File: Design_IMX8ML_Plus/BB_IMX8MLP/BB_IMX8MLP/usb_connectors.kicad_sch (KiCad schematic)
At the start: 29 parts, among them J9 GSB311231HR, P1 USB_C_Plug, U10 PCMF3USB3S, U9 PCMF3USB3S

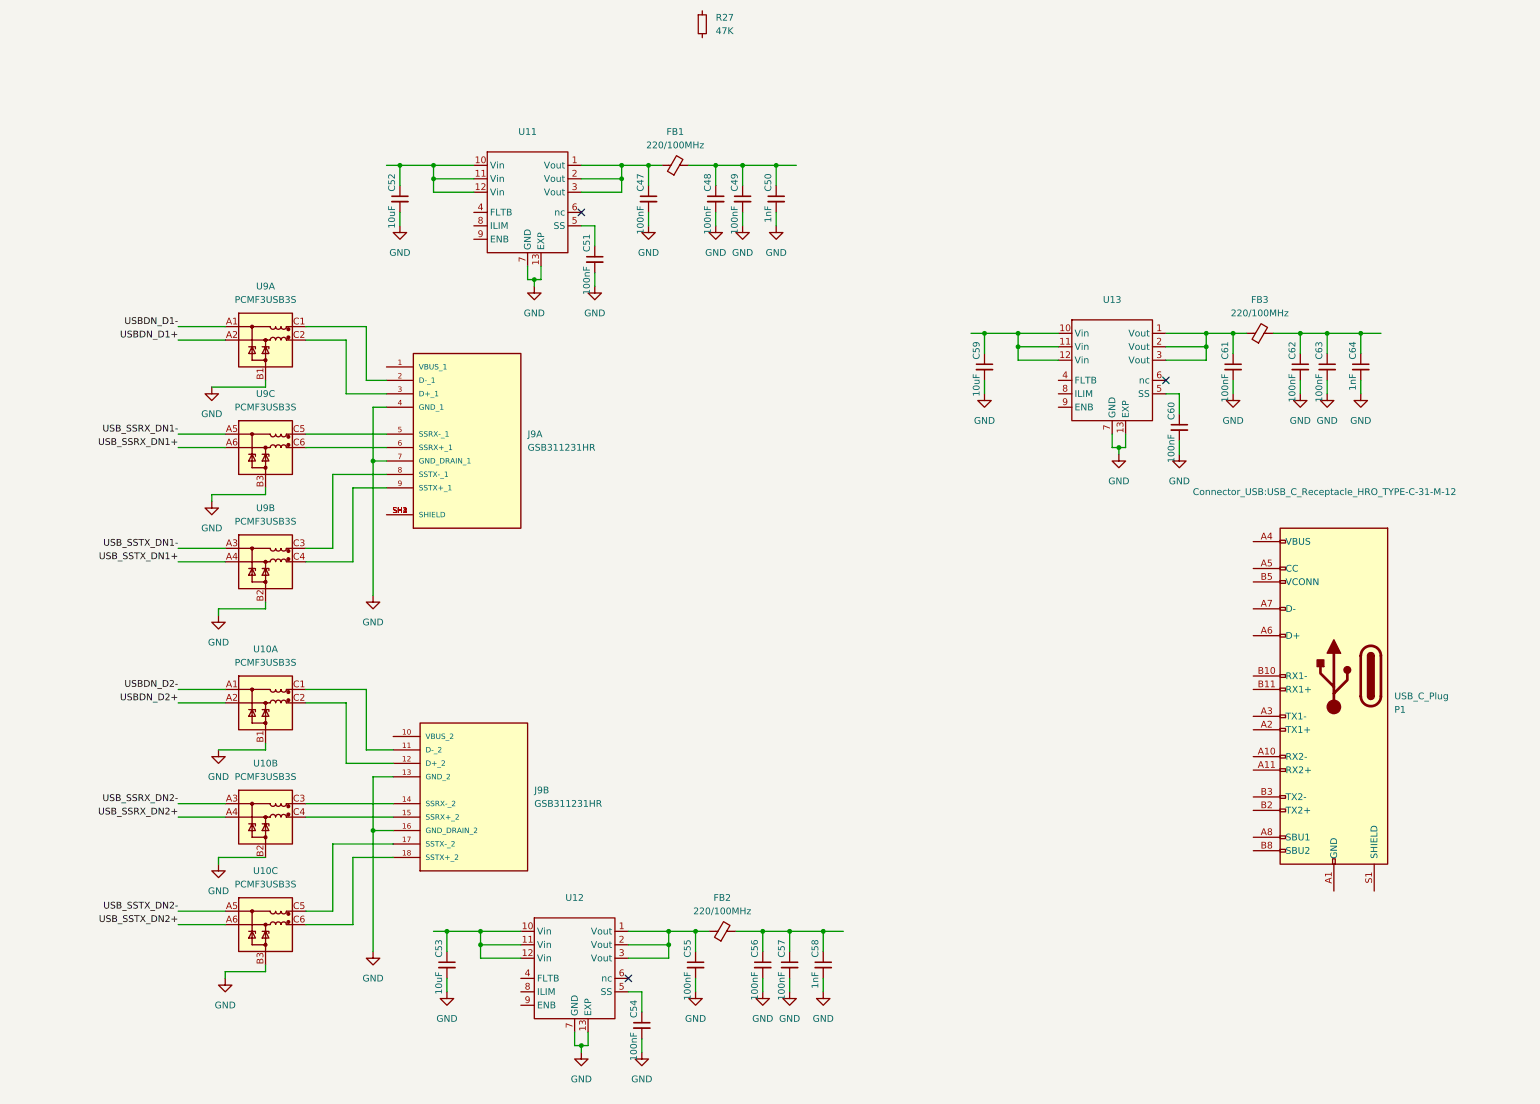
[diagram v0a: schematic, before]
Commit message: improving Ethernet, USB and Camera inteface
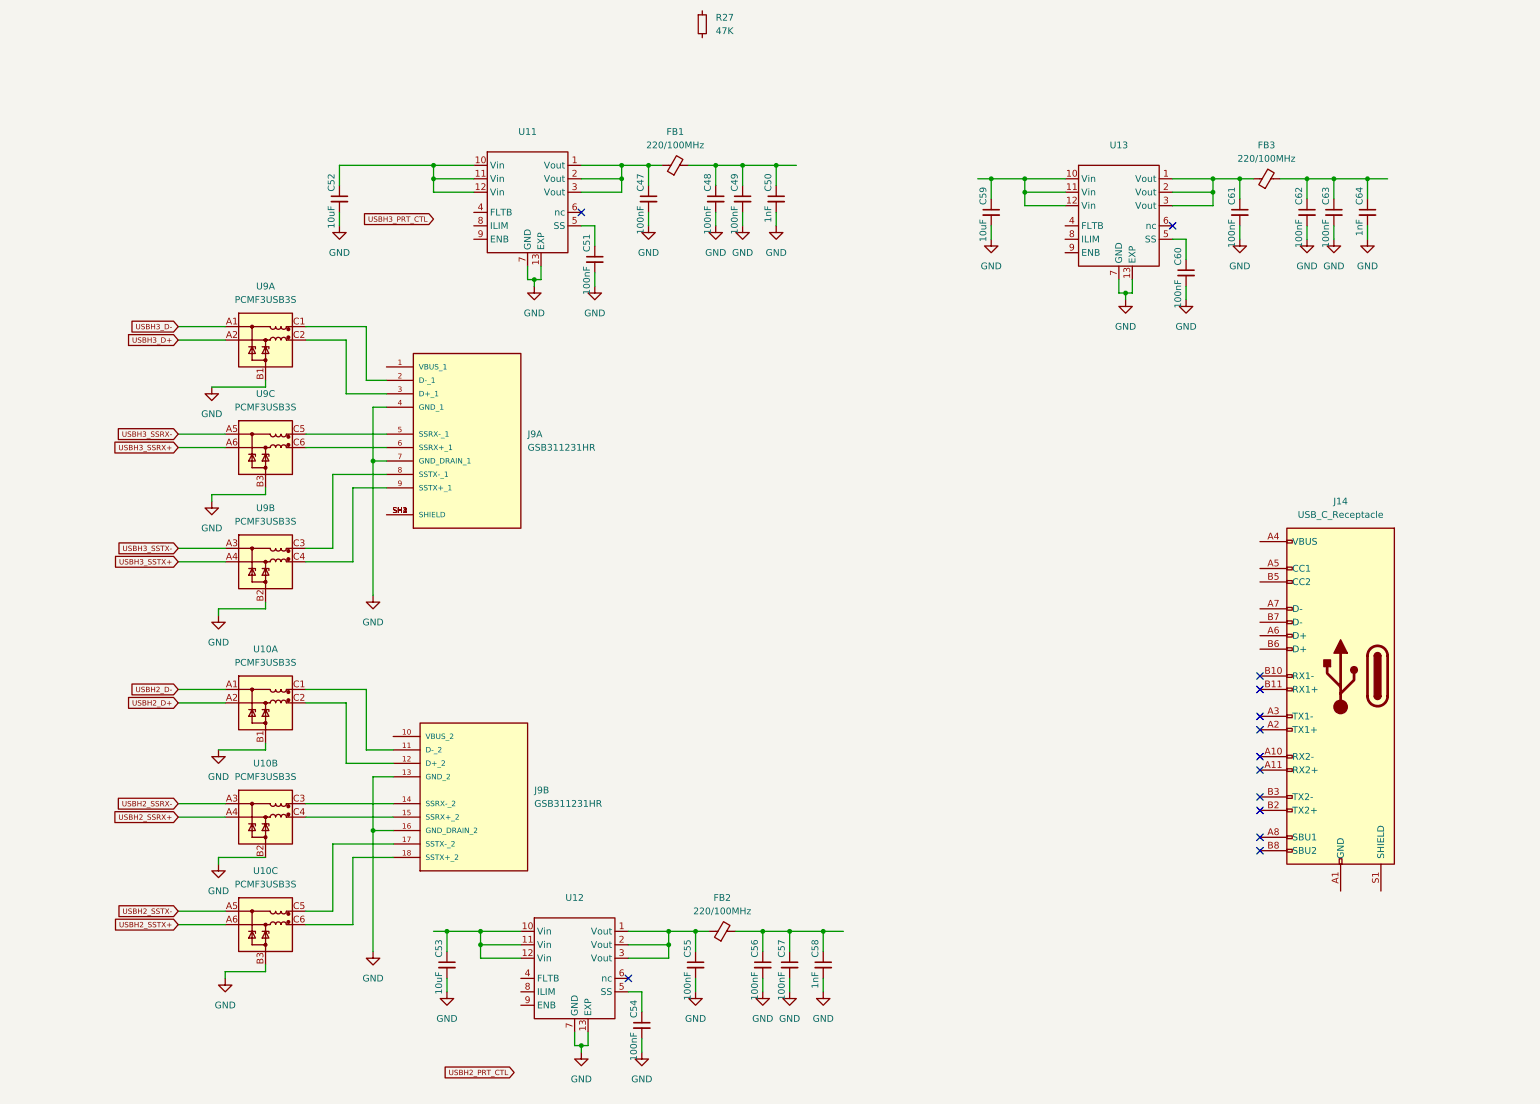
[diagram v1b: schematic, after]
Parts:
- removed P1: USB_C_Plug, Connector_USB:USB_C_Receptacle_HRO_TYPE-C-31-M-12, symbol Connector:USB_C_Plug
- added J14: USB_C_Receptacle, symbol Connector:USB_C_Receptacle
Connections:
- net USBDN_D1+ renamed USBH3_D+
- net USBDN_D1- renamed USBH3_D-
- net USBDN_D2+ renamed USBH2_D+
- net USBDN_D2- renamed USBH2_D-
- net USB_SSRX_DN1+ renamed USBH3_SSRX+
- net USB_SSRX_DN1- renamed USBH3_SSRX-
- net USB_SSRX_DN2+ renamed USBH2_SSRX+
- net USB_SSRX_DN2- renamed USBH2_SSRX-
- net USB_SSTX_DN1+ renamed USBH3_SSTX+
- net USB_SSTX_DN1- renamed USBH3_SSTX-
- net USB_SSTX_DN2+ renamed USBH2_SSTX+
- net USB_SSTX_DN2- renamed USBH2_SSTX-
- new net: J14.A1 (GND), J14.A12 (GND), J14.B1 (GND), J14.B12 (GND)
- new net: J14.A4 (VBUS), J14.A9 (VBUS), J14.B4 (VBUS), J14.B9 (VBUS)
- no-connect marks 3 -> 13
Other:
- moved on the sheet: C52, C59, C60, C61, C62, C63, C64, FB3, U13

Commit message: Review
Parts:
- added C150, C151, C152, C153: 100nF, Capacitor_SMD:C_0402_1005Metric, symbol Device:C_Small
- added R59, R60, R61: 0, Resistor_SMD:R_0402_1005Metric, symbol Device:R_Small
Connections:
- net USBH2_PRT_CTL: now also U12.8 (ILIM), R59.2
- net USBH2_SSTX+: now also C153.2; no longer U10.A6 (CH3_IN-)
- net USBH2_SSTX-: now also C152.2; no longer U10.A5 (CH3_IN+)
- net USBH3_PRT_CTL: now also U11.8 (ILIM), R60.2
- net USBH3_SSTX+: now also C151.2; no longer U9.A4 (CH2_IN-)
- net USBH3_SSTX-: now also C150.2; no longer U9.A3 (CH2_IN+)
- net at U13.4 (FLTB): now also R61.1
- net at U13.8 (ILIM): now also R61.2
- net VBUSH_2: now reaches C56.1, C57.1, C58.1, FB2.2
- net VBUSH_2: now also J9.10 (VBUS_2)
- net VBUSH_1: now reaches C48.1, C49.1, C50.1, FB1.2
- net VBUSH_1: now also J9.1 (VBUS_1)
- net VBUS: now reaches C62.1, C63.1, C64.1, FB3.2
- net VBUS: now also J14.A4 (VBUS), J14.A9 (VBUS), J14.B4 (VBUS), J14.B9 (VBUS)
- net at U11.4 (FLTB): now also R60.1
- net at U12.4 (FLTB): now also R59.1
- new net: C152.1, U10.A5 (CH3_IN+)
- new net: C153.1, U10.A6 (CH3_IN-)
- new net: C150.1, U9.A3 (CH2_IN+)
- new net: C151.1, U9.A4 (CH2_IN-)
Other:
- moved on the sheet: C53, C55, C56, C57, C58, FB2

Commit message: reorganization of the componentes
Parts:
- removed R27: 47K, Resistor_SMD:R_0402_1005Metric, symbol Device:R_Small
- added R16: 0, Resistor_SMD:R_0402_1005Metric, symbol Device:R_Small
- added U39: ~, symbol _W_MX8M:CBTU02043
- added U40, U41: PCMF3USB3S, Package_CSP:Nexperia_WLCSP-15_6-3-6_2.37x1.17mm_Layout6x3_P0.4mm, symbol Power_Protection:PCMF3USB3S
- J14: footprint (none) -> Connector_USB:USB_C_Receptacle_GCT_USB4110
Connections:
- net at J14.A10 (RX2-): now also U40.C5 (CH3_OUT+)
- net at J14.A11 (RX2+): now also U40.C6 (CH3_OUT-)
- net at J14.A2 (TX1+): now also U40.C4 (CH2_OUT-)
- net at J14.A3 (TX1-): now also U40.C3 (CH2_OUT+)
- net USBH1_D+: now reaches J14.A6 (D+)
- net USBH1_D+: now also J14.B6 (D+)
- net USBH1_D-: now reaches J14.A7 (D-)
- net USBH1_D-: now also J14.B7 (D-)
- net at J14.B10 (RX1-): now also U40.C1 (CH1_OUT+)
- net at J14.B11 (RX1+): now also U40.C2 (CH1_OUT-)
- net at J14.B2 (TX2+): now also U41.C2 (CH1_OUT-)
- net at J14.B3 (TX2-): now also U41.C1 (CH1_OUT+)
- net at R61.2: no longer U13.8 (ILIM)
- new net: U39.2 (B1_P), U40.A5 (CH3_IN+)
- new net: U39.1 (B1_N), U40.A6 (CH3_IN-)
- new net: U39.15 (B1_P), U41.A1 (CH1_IN+)
- new net: U39.16 (C1_N), U41.A2 (CH1_IN-)
- new net: U39.8 (B0_P), U40.A1 (CH1_IN+)
- new net: U39.7 (B0_N), U40.A2 (CH1_IN-)
- new net: U39.5 (C0_P), U40.A3 (CH2_IN+)
- new net: U39.6 (C0_N), U40.A4 (CH2_IN-)
- new net USBH1_SSRX+: U39.13 (A1_P)
- new net USBH1_SSRX-: U39.14 (A1_N)
- new net USBH1_SSTX+: U39.10 (A0_P)
- new net USBH1_SSTX-: U39.9 (A0_N)
- no-connect marks 13 -> 3

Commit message: pcb reorganization
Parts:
- removed FB1, FB2, FB3: 220/100MHz, Resistor_SMD:R_0603_1608Metric, symbol Device:FerriteBead_Small
- removed U39: ~, symbol _W_MX8M:CBTU02043
- removed U41: PCMF3USB3S, Package_CSP:Nexperia_WLCSP-15_6-3-6_2.37x1.17mm_Layout6x3_P0.4mm, symbol Power_Protection:PCMF3USB3S
- added L17, L18, L19: 2.2uH_12A, Inductor_SMD:L_1806_4516Metric, symbol Device:L_Small
- J14: footprint Connector_USB:USB_C_Receptacle_GCT_USB4110 -> Connector_USB:USB_C_Receptacle_Molex_105450-0101
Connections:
- net GND: no longer U10.B1 (GND_CH1), U10.B2 (GND_CH2), U10.B3 (GND_CH3), U9.B1 (GND_CH1), U9.B2 (GND_CH2), U9.B3 (GND_CH3)
- net USBH1_D+: now also U40.A5 (CH3_IN+); no longer J14.A6 (D+), J14.B6 (D+)
- net USBH1_D-: now also U40.A6 (CH3_IN-); no longer J14.A7 (D-), J14.B7 (D-)
- net USBH1_SSRX+: now also U40.A3 (CH2_IN+)
- net USBH1_SSRX-: now also U40.A4 (CH2_IN-)
- net USBH1_SSTX+: now also U40.A1 (CH1_IN+)
- net USBH1_SSTX-: now also U40.A2 (CH1_IN-)
- net USBH2_D+: now also U10.A1 (CH1_IN+); no longer U10.A2 (CH1_IN-)
- net USBH2_D-: now also U10.A2 (CH1_IN-); no longer U10.A1 (CH1_IN+)
- net USBH2_SSRX+: now also U10.A5 (CH3_IN+); no longer U10.A4 (CH2_IN-)
- net USBH2_SSRX-: now also U10.A6 (CH3_IN-); no longer U10.A3 (CH2_IN+)
- net USBH3_D+: now also U9.A1 (CH1_IN+); no longer U9.A2 (CH1_IN-)
- net USBH3_D-: now also U9.A2 (CH1_IN-); no longer U9.A1 (CH1_IN+)
- net USBH3_SSRX+: now also U9.A5 (CH3_IN+); no longer U9.A6 (CH3_IN-)
- net USBH3_SSRX-: now also U9.A6 (CH3_IN-); no longer U9.A5 (CH3_IN+)
- net VBUS: now also L18.2
- net VBUSH_1: now also L17.2
- net VBUSH_2: now also L19.2
- net at C152.1: now also U10.A4 (CH2_IN-); no longer U10.A5 (CH3_IN+)
- net at C153.1: now also U10.A3 (CH2_IN+); no longer U10.A6 (CH3_IN-)
- net USBH2SSRX+: now reaches U10.C5 (CH3_OUT+)
- net USBH2SSRX+: now also J9.15 (SSRX+_2); no longer J9.17 (SSTX-_2)
- net USBH2SSRX-: now reaches U10.C6 (CH3_OUT-)
- net USBH2SSRX-: now also J9.14 (SSRX-_2); no longer J9.18 (SSTX+_2)
- net at U9.A3 (CH2_IN+): now also C151.1; no longer C150.1
- net at U9.A4 (CH2_IN-): now also C150.1; no longer C151.1
- net USBH3SSTX+: now reaches U9.C3 (CH2_OUT+)
- net USBH3SSTX+: now also J9.9 (SSTX+_1); no longer J9.8 (SSTX-_1)
- net USBH3SSTX-: now reaches U9.C4 (CH2_OUT-)
- net USBH3SSTX-: now also J9.8 (SSTX-_1); no longer J9.9 (SSTX+_1)
- net USBH2D+: now reaches U10.C1 (CH1_OUT+)
- net USBH2D+: now also J9.12 (D+_2); no longer J9.11 (D-_2)
- net USBH2D-: now reaches U10.C2 (CH1_OUT-)
- net USBH2D-: now also J9.11 (D-_2); no longer J9.12 (D+_2)
- net USBH2SSTX+: now reaches U10.C3 (CH2_OUT+)
- net USBH2SSTX+: now also J9.18 (SSTX+_2); no longer J9.14 (SSRX-_2)
- net USBH2SSTX-: now reaches U10.C4 (CH2_OUT-)
- net USBH2SSTX-: now also J9.17 (SSTX-_2); no longer J9.15 (SSRX+_2)
- net at C47.1, U11.1 (Vout), U11.2 (Vout)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: now also L17.1
- net USBH3SSRX+: now reaches U9.C5 (CH3_OUT+)
- net USBH3SSRX+: now also J9.6 (SSRX+_1); no longer J9.5 (SSRX-_1)
- net USBH3SSRX-: now reaches U9.C6 (CH3_OUT-)
- net USBH3SSRX-: now also J9.5 (SSRX-_1); no longer J9.6 (SSRX+_1)
- net at C61.1, U13.1 (Vout), U13.2 (Vout)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: now also L18.1
- net at J14.A10 (RX2-): no longer U40.C5 (CH3_OUT+)
- net at J14.A11 (RX2+): no longer U40.C6 (CH3_OUT-)
- net USBH1SSRX-: now reaches U40.C4 (CH2_OUT-)
- net USBH1SSRX-: now also J14.B10 (RX1-); no longer J14.A2 (TX1+)
- net USBH1SSRX+: now reaches U40.C3 (CH2_OUT+)
- net USBH1SSRX+: now also J14.B11 (RX1+); no longer J14.A3 (TX1-)
- net USBH1SSTX+: now reaches U40.C1 (CH1_OUT+)
- net USBH1SSTX+: now also J14.A2 (TX1+); no longer J14.B10 (RX1-)
- net USBH1SSTX-: now reaches U40.C2 (CH1_OUT-)
- net USBH1SSTX-: now also J14.A3 (TX1-); no longer J14.B11 (RX1+)
- net USBH3D+: now reaches U9.C1 (CH1_OUT+)
- net USBH3D+: now also J9.3 (D+_1); no longer J9.2 (D-_1)
- net USBH3D-: now reaches U9.C2 (CH1_OUT-)
- net USBH3D-: now also J9.2 (D-_1); no longer J9.3 (D+_1)
- net at C55.1, U12.1 (Vout), U12.2 (Vout)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: now also L19.1
- new net USBH1D+: J14.A6 (D+), J14.B6 (D+), U40.C5 (CH3_OUT+)
- new net USBH1D-: J14.A7 (D-), J14.B7 (D-), U40.C6 (CH3_OUT-)
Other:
- moved on the sheet: C150, C151, J14, U10A, U10B, U10C, U40A, U40B, U40C, U9A, U9B, U9C

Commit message: CPU Board actualizate
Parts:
- removed C62, C63: 100nF, Capacitor_SMD:C_0402_1005Metric, symbol Device:C_Small
- removed R16: 0, Resistor_SMD:R_0402_1005Metric, symbol Device:R_Small
- added C194, C195: 100uF, Capacitor_SMD:C_1210_3225Metric_Pad1.33x2.70mm_HandSolder, symbol Device:C_Small
- C48, C49, C56, C57: value 100nF -> 100uF; footprint Capacitor_SMD:C_0402_1005Metric -> Capacitor_SMD:C_1210_3225Metric_Pad1.33x2.70mm_HandSolder
- C52, C53, C59: footprint Capacitor_SMD:C_0402_1005Metric -> Capacitor_SMD:C_0603_1608Metric_Pad1.08x0.95mm_HandSolder
- J9: footprint _W_SBC:AMPHENOL_GSB311231HR -> GSB311231HR:AMPHENOL_GSB311231HR
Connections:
- net GND: now also C194.2, C195.2
- net VBUS: now also C48.1, C49.1
- net VBUSH_1: now also C194.1, C195.1; no longer C48.1, C49.1
- net 5V_BB: now reaches C52.1, U11.10 (Vin), U11.11 (Vin), U11.12 (Vin)
- net 5V_BB: now also C53.1, C59.1, U12.10 (Vin), U12.11 (Vin), U12.12 (Vin), U13.10 (Vin), U13.11 (Vin), U13.12 (Vin)
- net at R61.2: now also U13.8 (ILIM)

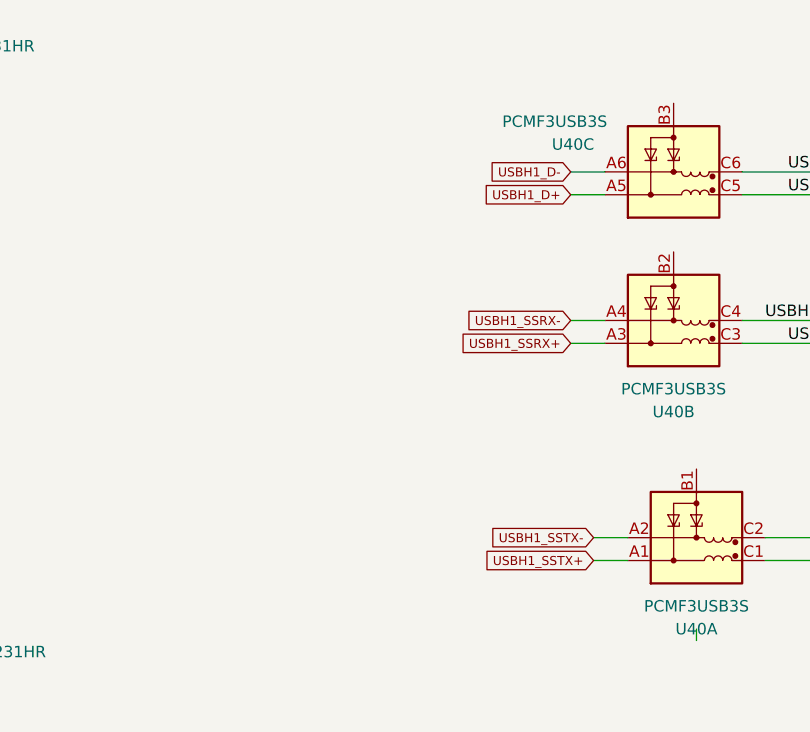
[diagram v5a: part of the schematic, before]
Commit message: [PROCESSOR] Create zones It added power zones in the four layer
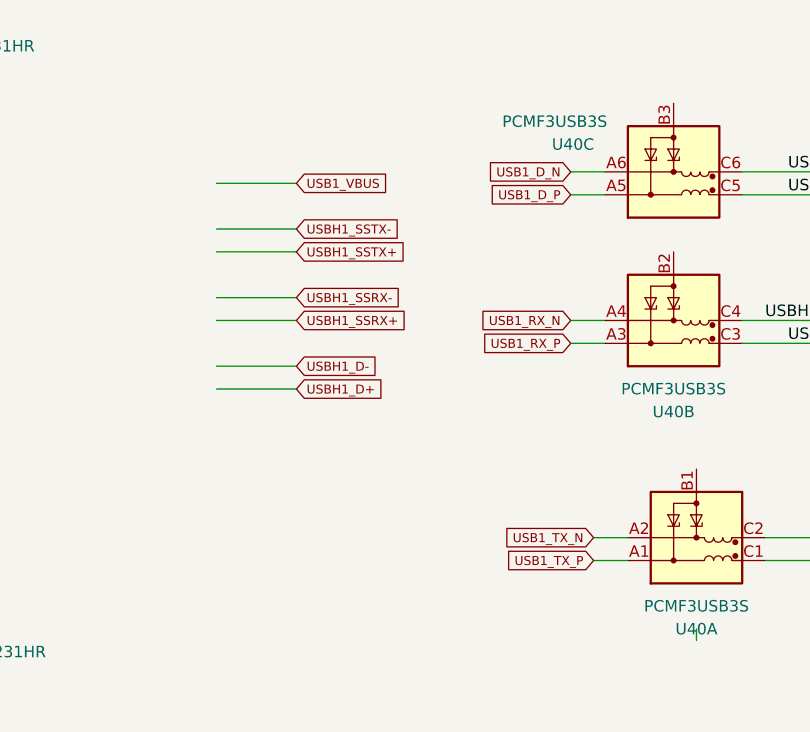
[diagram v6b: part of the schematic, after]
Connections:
- net USBH1_D+: no longer U40.A5 (CH3_IN+)
- net USBH1_D-: no longer U40.A6 (CH3_IN-)
- net USBH1_SSRX+: no longer U40.A3 (CH2_IN+)
- net USBH1_SSRX-: no longer U40.A4 (CH2_IN-)
- net USBH1_SSTX+: no longer U40.A1 (CH1_IN+)
- net USBH1_SSTX-: no longer U40.A2 (CH1_IN-)
- new net USB1_D_N: U40.A6 (CH3_IN-)
- new net USB1_D_P: U40.A5 (CH3_IN+)
- new net USB1_RX_N: U40.A4 (CH2_IN-)
- new net USB1_RX_P: U40.A3 (CH2_IN+)
- new net USB1_TX_N: U40.A2 (CH1_IN-)
- new net USB1_TX_P: U40.A1 (CH1_IN+)
